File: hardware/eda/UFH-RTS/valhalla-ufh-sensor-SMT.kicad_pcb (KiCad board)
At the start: 2 copper layers, 99.6 x 64.3 mm, 55 parts, among them J1 K-TC, J2 RTD, J3 NTC, J4 1-W, J5 ModBUS, J6 ICSP, J7 MAINS, U1 ATmega328PB-A, U2 MAX31865xAP, U3 MAX31856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

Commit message: BUGFIX: The Round Tracks plugin ignores design rules  - all tracks touched by the plugin will need to be rerouted, this commit    marks the beginning of that effort.
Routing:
- net VCC: track 21.0 -> 9.32 mm, vias 3 -> 0
- net GND: track 53.6 -> 42.5 mm, vias 33 -> 31

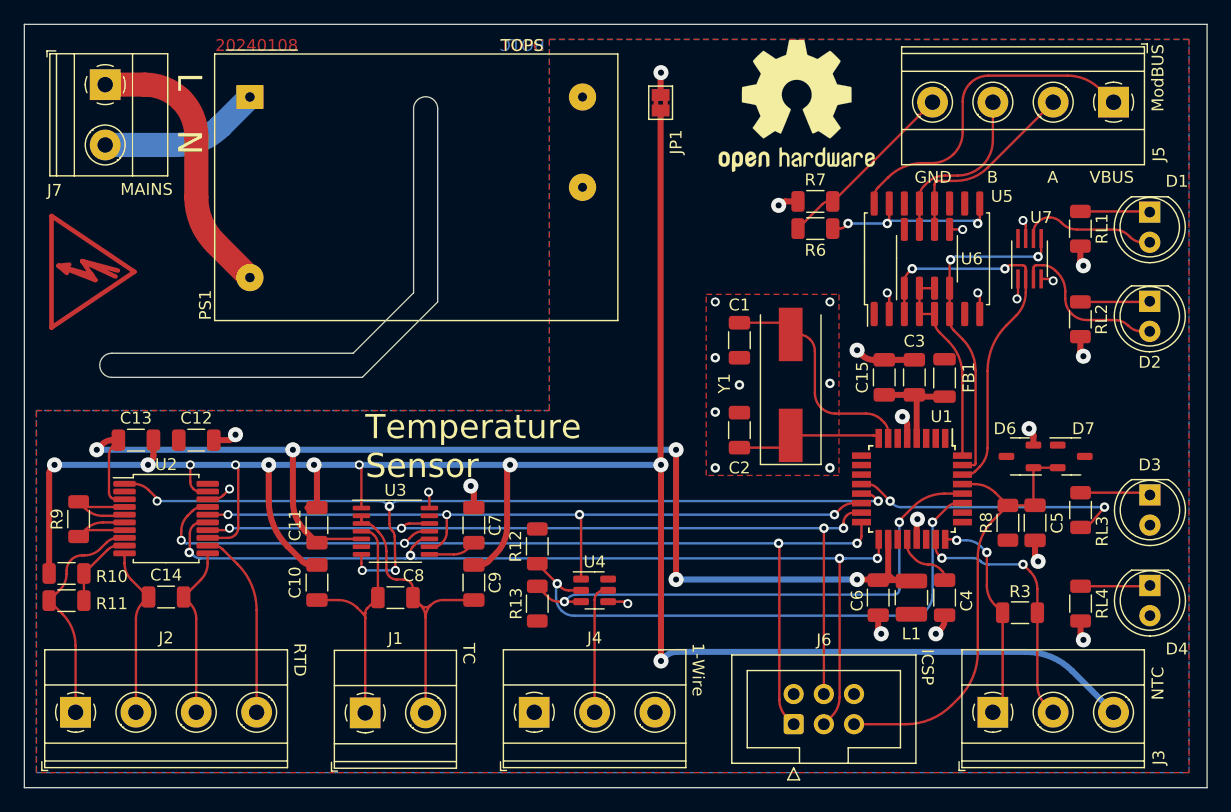
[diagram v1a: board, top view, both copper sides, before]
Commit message: BUGFIX: done cleaning-up after curved track plugin   - also switched to 2-pin terminal block for the NTC (there's no use really     in exposing the measurement power signal)
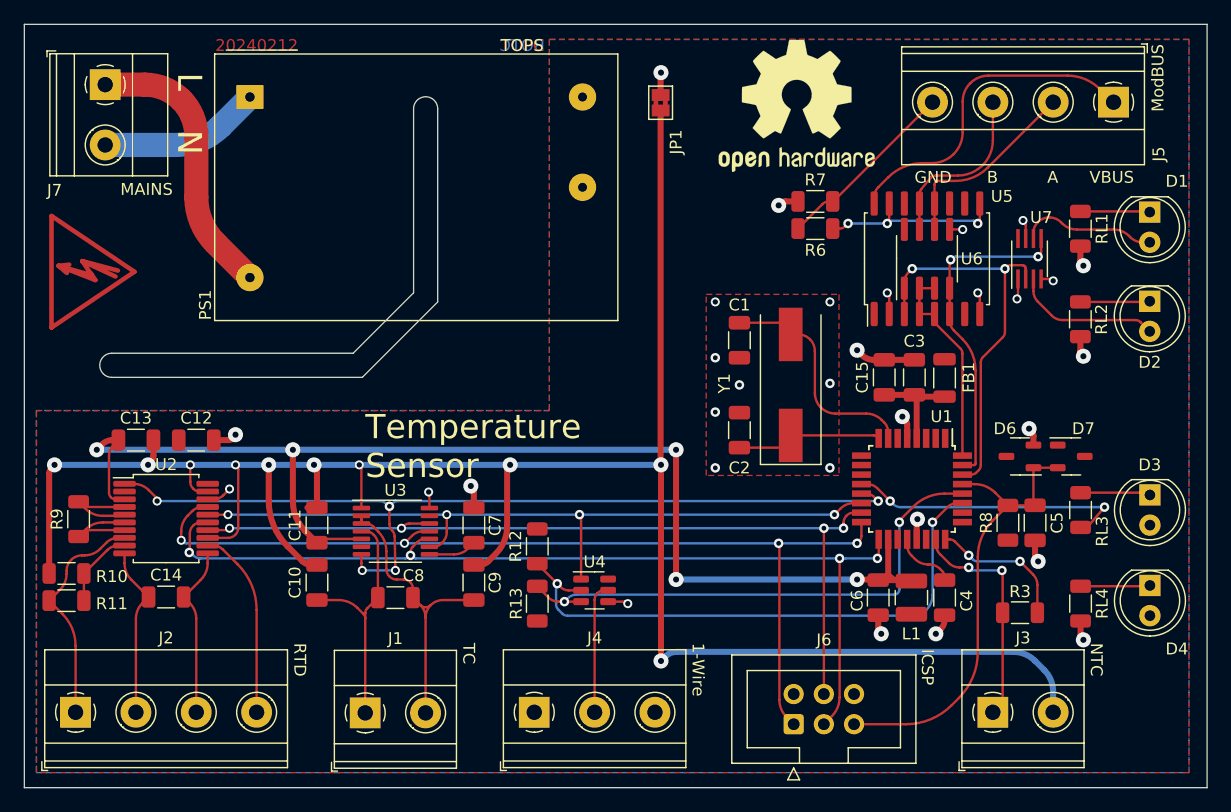
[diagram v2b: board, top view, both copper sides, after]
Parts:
- J3: footprint TerminalBlock_Phoenix:TerminalBlock_Phoenix_MKDS-1,5-3-5.08_1x03_P5.08mm_Horizontal -> TerminalBlock_Phoenix:TerminalBlock_Phoenix_MKDS-1,5-2-5.08_1x02_P5.08mm_Horizontal
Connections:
- J3 pad 2: Net-(J3-Pin_2) -> GNDA
- R3 pad 2: Net-(J3-Pin_2) -> Net-(U1-PC1)
- U1 pad 23: Net-(J3-Pin_2) -> Net-(J3-Pin_1)
- U1 pad 24: Net-(J3-Pin_1) -> Net-(U1-PC1)
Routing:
- net Net-(J3-Pin_2): track 22.0 -> 0.00 mm, vias 2 -> 0
- net Net-(U1-PC1): track 0.00 -> 11.9 mm, vias 0 -> 2
- net GNDA: track 189.2 -> 185.8 mm
- net Net-(D2-A): track 14.0 -> 12.4 mm
- net Net-(J3-Pin_1): track 16.9 -> 18.2 mm
- net Net-(U1-PD0): track 33.3 -> 34.0 mm
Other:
- board text added: "20240212"
- board text removed: "20240108"

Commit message: UPDATE: upgraded to latest KiCAD version and cosmetic adjustments
  - moved Dalas 1-Wire bridge up on UFH Sensor PCB to align with the
    other temperature sensor chips.
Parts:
- moved U4 3.91 mm to (73.7, 92.2)
- moved R12 1.79 mm to (69.0, 90.7)
- moved R13 1.79 mm to (69.0, 95.5)
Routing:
- net Net-(U1-PB2): track 64.5 -> 59.7 mm
- net Net-(U1-PB0): track 23.9 -> 19.4 mm
- net Net-(J4-Pin_2): track 11.0 -> 15.4 mm
- net Net-(U1-PB1): track 75.7 -> 72.2 mm
- net Net-(J5-Pin_1): track 27.9 -> 25.8 mm
- net GNDA: track 185.8 -> 183.9 mm
- net Net-(J6-Pin_1): track 81.1 -> 79.3 mm
- net Net-(U1-PC4): track 48.9 -> 47.2 mm
- net /AVCC: track 103.9 -> 102.2 mm
- net Net-(J1-Pin_2): track 25.2 -> 24.0 mm
- net /RS485_P: track 14.8 -> 13.6 mm
- net Net-(U1-XTAL1/PB6): track 18.1 -> 17.0 mm
- net Net-(D1-A): track 11.6 -> 10.4 mm
- net Net-(J6-Pin_3): track 80.8 -> 79.9 mm
- net GND: track 42.5 -> 41.6 mm
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
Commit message: UPDATE: fixed connection of AREF on UFH CPU
 - according to official documentation, ATMega's AREF pin should be
   connected only to a decoupling capacitor. If/when AREF=AVCC is
   desired for an ADC measurement, they can be connected together
   internally via register settings.
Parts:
- removed the REF** at (90.7, 55.4)
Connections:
- C4 pad 1: VCC -> Net-(U1-AREF)
- U1 pad 20: VCC -> Net-(U1-AREF)
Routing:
- net Net-(J4-Pin_2): track 15.4 -> 0.36 mm
- net Net-(U1-AREF): track 0.00 -> 5.26 mm
- net Net-(U1-PB0): track 19.4 -> 23.9 mm
- net VCC: track 8.54 -> 4.07 mm
- net Net-(U1-PB1): track 72.2 -> 75.7 mm
- net Net-(J5-Pin_1): track 25.8 -> 27.9 mm
- net GNDA: track 183.9 -> 185.8 mm
- net Net-(J6-Pin_1): track 79.3 -> 81.1 mm
- net /AVCC: track 102.2 -> 103.9 mm
- net Net-(U1-PC4): track 47.2 -> 48.6 mm
- net Net-(J1-Pin_2): track 24.0 -> 25.2 mm
- net /RS485_P: track 13.6 -> 14.8 mm
- net Net-(U1-XTAL1/PB6): track 17.0 -> 18.1 mm
- net Net-(U1-PB2): track 59.7 -> 60.8 mm
- net Net-(D1-A): track 10.4 -> 11.6 mm
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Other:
- board text added: "20250105"
- board text removed: "20240212"
